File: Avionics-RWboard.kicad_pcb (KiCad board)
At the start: 2 copper layers, 90.2 x 95.9 mm, 108 parts, among them J1 282834-2, J2 200528-0100, Q1 NX3008NBKS, Q10 MBT2222ADW1T1, Q11 NX3008NBKS, Q12 MBT2222ADW1T1, Q2 MBT2222ADW1T1, Q3 NX3008NBKS, Q4 MBT2222ADW1T1, Q5 IRLML2803, Q9 NX3008NBKS, U2 TPS259621DDA, U4 ADM1176-1ARMZ-R7

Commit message: Layout mostly complete
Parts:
- removed C29: 10u, Capacitor_SMD:C_1206_3216Metric_Pad1.33x1.80mm_HandSolder
- removed kibuzzard-67C0A908: G***, kibuzzard-67C0A908
- added C31: 10uF, Capacitor_SMD:C_0603_1608Metric, F.Cu at (156.6, 113.5)
- added C36: 10uF, Capacitor_SMD:C_0603_1608Metric, F.Cu at (157.5, 119.5)
- added D8: ESD9X3.3ST5G, Diode_SMD:D_SOD-923, F.Cu at (157.9, 123.0)
- added L1: 1UH, Argus_RW_Library:HCM1A1104V2, F.Cu at (152.9, 77.0)
- added M1: ~, Argus_RW_Library:Reaction_Wheel, B.Cu at (138.1, 93.6)
- added Q6: SiRA99DP, Argus-Miscellaneous:PowerPAK SO-8, F.Cu at (142.4, 63.9)
- added R18: 0R, Resistor_SMD:R_0402_1005Metric_Pad0.72x0.64mm_HandSolder, F.Cu at (133.0, 127.5)
- added R19: 0R, Resistor_SMD:R_0402_1005Metric_Pad0.72x0.64mm_HandSolder, F.Cu at (132.4, 128.1)
- added R51: 0R, Resistor_SMD:R_0603_1608Metric, F.Cu at (157.5, 121.5)
- added R52: 0R, Resistor_SMD:R_2512_6332Metric_Pad1.40x3.35mm_HandSolder, F.Cu at (130.9, 60.5)
- added R53: 0R, Resistor_SMD:R_2512_6332Metric_Pad1.40x3.35mm_HandSolder, F.Cu at (156.4, 60.5)
- added R54: 0R, Resistor_SMD:R_0402_1005Metric_Pad0.72x0.64mm_HandSolder, F.Cu at (142.4, 94.2)
- added R55: 0R, Resistor_SMD:R_0402_1005Metric_Pad0.72x0.64mm_HandSolder, F.Cu at (142.4, 95.3)
- added R56: 0R, Resistor_SMD:R_0402_1005Metric_Pad0.72x0.64mm_HandSolder, F.Cu at (142.1, 71.6)
- added R57: 0R, Resistor_SMD:R_0402_1005Metric_Pad0.72x0.64mm_HandSolder, F.Cu at (141.5, 71.0)
- added R58: 0R, Resistor_SMD:R_0402_1005Metric_Pad0.72x0.64mm_HandSolder, F.Cu at (150.1, 91.8)
- added TP1: ~, Argus_RW_Library:KEYSTONE_5001, F.Cu at (162.9, 60.5)
- added TP10: ~, Argus_RW_Library:KEYSTONE_5001, F.Cu at (144.0, 86.5)
- added TP11: ~, Argus_RW_Library:KEYSTONE_5001, F.Cu at (158.3, 126.5)
- added TP2: ~, Argus_RW_Library:KEYSTONE_5001, F.Cu at (149.1, 60.5)
- added TP3: ~, Argus_RW_Library:KEYSTONE_5001, F.Cu at (137.5, 60.5)
- added TP4: ~, Argus_RW_Library:KEYSTONE_5001, F.Cu at (119.3, 60.5)
- added TP5: ~, Argus_RW_Library:KEYSTONE_5001, F.Cu at (158.0, 109.6)
- added TP6: ~, Argus_RW_Library:KEYSTONE_5001, F.Cu at (139.0, 111.0)
- added TP7: ~, Argus_RW_Library:KEYSTONE_5001, F.Cu at (139.8, 86.5)
- added TP8: ~, Argus_RW_Library:KEYSTONE_5001, F.Cu at (126.9, 133.0)
- added TP9: ~, Argus_RW_Library:KEYSTONE_5001, F.Cu at (147.3, 86.5)
- added U1: MCF8315C1VQRGFRQ1, Argus_RW_Library:VQFN40_RGF_TEX, F.Cu at (148.4, 95.8)
- added U3: NCP730BMT330TBG, Argus_RW_Library:WDFN6-2x2_511BR_OSI, F.Cu at (157.4, 116.5)
- F1: value 2000mA -> 3000mA
- R14, R26: value 10k -> 0R; footprint Resistor_SMD:R_0603_1608Metric -> Resistor_SMD:R_0402_1005Metric_Pad0.72x0.64mm_HandSolder
- R24, R25, R31, R46, R47: footprint Resistor_SMD:R_0603_1608Metric -> Resistor_SMD:R_0402_1005Metric_Pad0.72x0.64mm_HandSolder
- R32: value 0.05R -> 0.01R
- moved R9 145.7 mm to (119.3, 108.1), turned to 90 degrees
- moved R11 145.2 mm to (119.3, 103.2), turned to -90 degrees
- moved R12 143.5 mm to (121.2, 109.8), turned to -90 degrees
- moved R10 142.3 mm to (122.2, 96.5), turned to 180 degrees
- moved R8 138.5 mm to (122.2, 98.5), turned to 180 degrees
- moved R7 138.5 mm to (122.0, 104.0)
- moved U2 137.0 mm to (120.4, 71.1), turned to -90 degrees
- moved C2 134.0 mm to (123.0, 109.8), turned to -90 degrees
- moved J2 133.2 mm to (138.1, 131.2)
- moved R37 132.2 mm to (99.4, 103.1), turned to -90 degrees
- moved R4 131.4 mm to (129.3, 103.1), turned to -90 degrees
- moved R38 130.9 mm to (101.3, 109.8), turned to -90 degrees
- moved Q4 130.4 mm to (122.2, 101.1), turned to 180 degrees
- moved Q3 130.3 mm to (122.1, 106.6)
- moved R5 129.9 mm to (131.2, 109.8), turned to -90 degrees
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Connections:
- net Net-(D5-K) renamed /Power/SWITCHED_POWER
- net Net-(Q6-S) renamed /Power/FUSED_POWER
- net SYSTEM_VDD renamed VMAIN
- C6 pad 2: Net-(U2-OUT) -> /Power/eFUSED_POWER
- J2 pad 1: GND -> SYS_3V3
- R24 pad 1: GND -> /Power/eFUSED_POWER
- R25 pad 2: /Power/A1 -> /Power/A0
- R26 pad 1: AGND -> /Motor/BRAKE
- R26 pad 2: /Motor/DIR -> AVDD
- R32 pad 1: VM -> /Power/MON_POWER
- R32 pad 2: Net-(U2-OUT) -> /Power/eFUSED_POWER
- R33 pad 1: VM -> /Power/MON_POWER
- U2 pad 5: Net-(U2-OUT) -> /Power/eFUSED_POWER
- U4 pad 1: Net-(U2-OUT) -> /Power/eFUSED_POWER
- U4 pad 2: VM -> /Power/MON_POWER
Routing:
- net GND: track 0.00 -> 99.4 mm, vias 0 -> 77
- net /Connectors/RW_EN: track 0.00 -> 86.4 mm, vias 0 -> 2
- net VM: track 0.00 -> 84.4 mm
- net /Connectors/SCL: track 0.00 -> 75.1 mm
- net /Power/I2C Bus Protection 2/SCL_DEVICE: track 0.00 -> 72.0 mm, vias 0 -> 2
- net /Power/I2C Bus Protection 2/SDA_DEVICE: track 0.00 -> 64.7 mm, vias 0 -> 2
- net /Power/eFUSED_POWER: track 0.00 -> 63.3 mm
- net /Connectors/RW_POWER_FLT: track 0.00 -> 58.9 mm, vias 0 -> 2
- net /Connectors/SDA: track 0.00 -> 57.1 mm, vias 0 -> 2
- net /Motor/I2C Bus Protection 1/SDA_DEVICE: track 0.00 -> 48.7 mm, vias 0 -> 2
- net LOCAL_3V3: track 0.00 -> 43.0 mm
- net /Motor/I2C Bus Protection 1/SCL_DEVICE: track 0.00 -> 39.0 mm, vias 0 -> 2
- net /Connectors/RW_MOTOR_FLT: track 0.00 -> 38.0 mm, vias 0 -> 1
- net /Power/SWITCHED_POWER: track 0.00 -> 34.1 mm
- net /Connectors/RW_MOTOR_ALRM: track 0.00 -> 33.0 mm, vias 0 -> 2
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- added copper zone on In2.Cu, net +3V3
- added copper zone on F.Cu, net /Motor/SW_BUCK
- added copper zone on B.Cu, net AGND
- added copper zone on F.Cu, net AGND
- added copper zone on In1.Cu, net AGND
- added copper zone on In2.Cu, net AGND
- added copper zone on In2.Cu, net AVDD
- added copper zone on B.Cu, net GND
- added copper zone on F.Cu, net GND
- added copper zone on In1.Cu, net GND
- added copper zone on In2.Cu, net GND
- added copper zone on B.Cu, net Net-(M1-A)
- added copper zone on F.Cu, net Net-(M1-A)
- added copper zone on B.Cu, net Net-(M1-B)
- added copper zone on F.Cu, net Net-(M1-B)
- added copper zone on B.Cu, net Net-(M1-C)
- added copper zone on F.Cu, net Net-(M1-C)
- added copper zone on F.Cu, net VM
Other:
- copper layers 2 -> 4
- board text added: "ARGUS Cubesat Carnegie Mellon University Reaction Wheel Board V1.0"
- board text added: "Reaction Wheel Board V1.0"
- board text removed: "ARGUS Cubesat Carnegie Mellon University Mainboard v3.0"
- board text removed: "mainboard.v3.0"

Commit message: Update silkscreen
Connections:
- U1 pad 39: unconnected-(U1-ALARM-Pad39) -> /Connectors/RW_MOTOR_ALRM
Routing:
- net /Connectors/RW_MOTOR_ALRM: track 33.0 -> 40.2 mm
- net unconnected-(U1-ALARM-Pad39): track 5.82 -> 0.00 mm
- net GND: track 99.4 -> 102.5 mm
- net AGND: track 30.0 -> 30.5 mm, vias 5 -> 12
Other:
- board text removed: "Reaction Wheel Board V1.0"

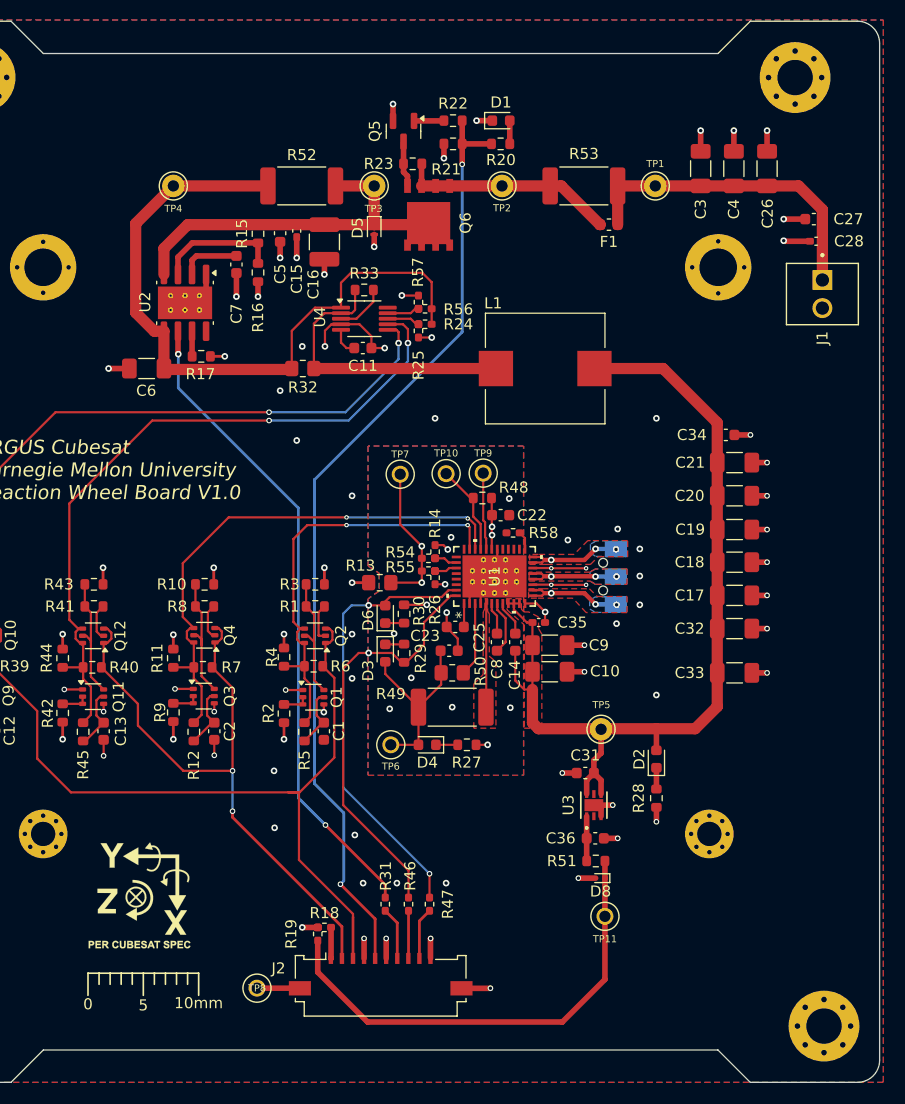
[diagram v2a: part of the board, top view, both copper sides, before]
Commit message: Push requested changes - silkscreen, copper width, pi filter
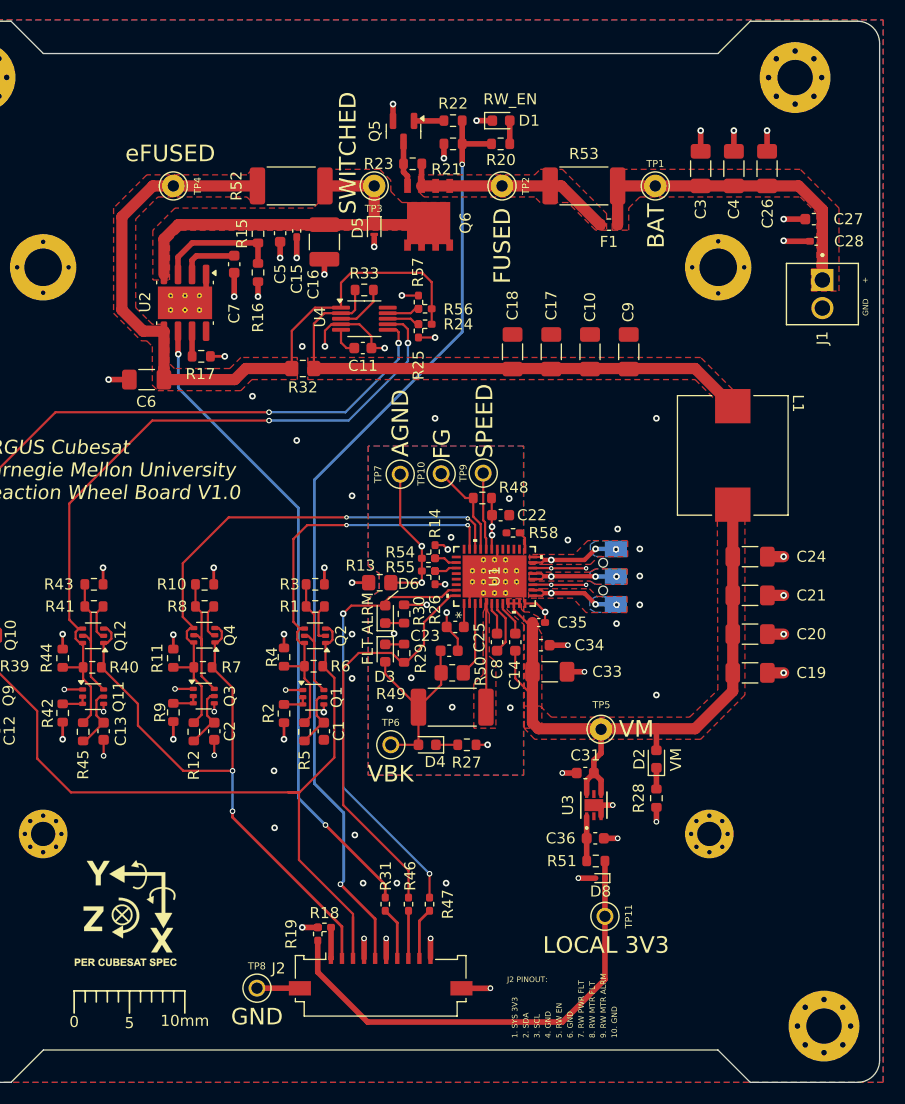
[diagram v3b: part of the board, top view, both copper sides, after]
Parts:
- removed C32: 47u, Capacitor_SMD:C_1206_3216Metric_Pad1.33x1.80mm_HandSolder
- added C24: 47u, Capacitor_SMD:C_1206_3216Metric_Pad1.33x1.80mm_HandSolder, F.Cu at (171.5, 94.0)
- moved C10 29.1 mm to (157.0, 75.5), turned to -90 degrees
- moved C18 27.6 mm to (150.0, 75.5), turned to -90 degrees
- moved C17 27.5 mm to (153.5, 75.5), turned to -90 degrees
- moved C9 27.5 mm to (160.5, 75.5), turned to -90 degrees
- moved C34 25.3 mm to (152.6, 102.0)
- moved L1 18.7 mm to (169.9, 84.8), turned to -90 degrees
- moved C33 16.7 mm to (153.4, 104.4)
- moved C19 13.0 mm to (171.5, 104.5)
- moved C20 12.6 mm to (171.5, 101.0)
- moved C21 12.1 mm to (171.5, 97.5)
- moved REF** 2.03 mm to (115.0, 126.2)
- moved REF** 2.03 mm to (110.4, 133.2)
- moved REF** 1.63 mm to (99.7, 93.5)
- moved C6 1.00 mm to (116.9, 78.0)
- moved R52 0.95 mm to (130.0, 60.5)
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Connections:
- C10 pad 2: VM -> /Power/MON_POWER
- C17 pad 2: VM -> /Power/MON_POWER
- C18 pad 2: VM -> /Power/MON_POWER
- C9 pad 2: VM -> /Power/MON_POWER
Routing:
- net /Power/MON_POWER: track 26.5 -> 49.4 mm
- net VM: track 84.4 -> 71.1 mm
- net GND: track 102.5 -> 97.5 mm, vias 77 -> 73
- net /Power/eFUSED_POWER: track 63.3 -> 66.4 mm
- net /Power/SWITCHED_POWER: track 34.1 -> 35.6 mm
- net /Motor/FG: track 8.27 -> 9.17 mm
- net /Connectors/RW_MOTOR_FLT: vias 1 -> 0
- added copper zone on F.Cu, net /Power/FUSED_POWER
- added copper zone on F.Cu, net /Power/MON_POWER
- added copper zone on F.Cu, net /Power/SWITCHED_POWER
- added copper zone on F.Cu, net /Power/eFUSED_POWER
- added copper zone on F.Cu, net VMAIN
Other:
- board text added: "+"
- board text added: "1. SYS 3V3"
- board text added: "10. GND"
- board text added: "2. SDA"
- board text added: "3. SCL"
- board text added: "4. GND"
- board text added: "5. RW EN"
- board text added: "6. GND"
- board text added: "7. RW PWR FLT"
- board text added: "8. RW MTR FLT"
- board text added: "9. RW MTR ALRM"
- board text added: "AGND"
- board text added: "ALRM"
- board text added: "BAT"
- board text added: "FG"
- board text added: "FLT"
- board text added: "FUSED"
- board text added: "GND"
- board text added: "J2 PINOUT:"
- board text added: "LOCAL 3V3"
- board text added: "RW_EN"
- board text added: "SPEED"
- board text added: "SWITCHED"
- board text added: "VBK"
- board text added: "VM"
- board text added: "eFUSED"

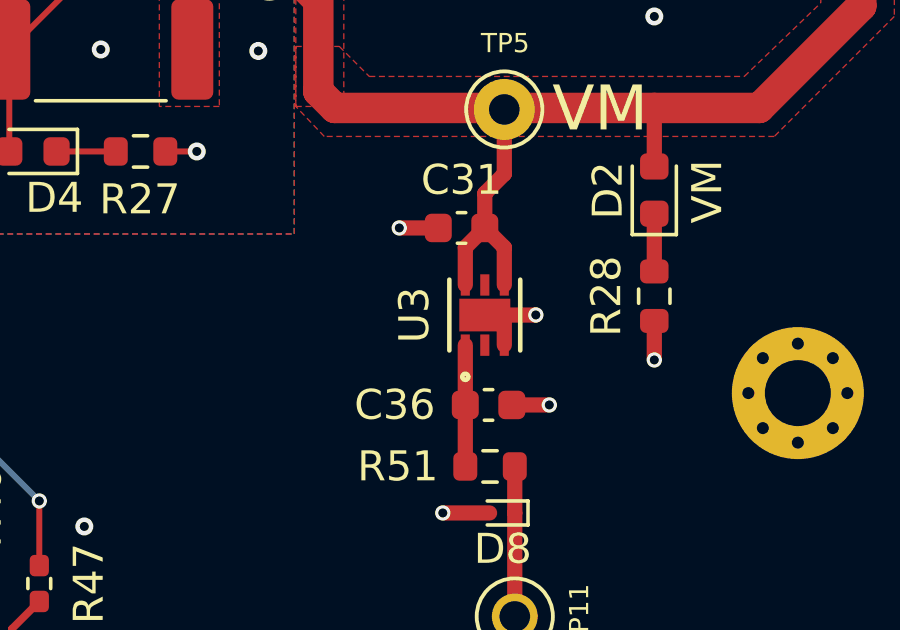
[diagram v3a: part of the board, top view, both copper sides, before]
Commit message: Add and correct BOM for easy Digikey ordering
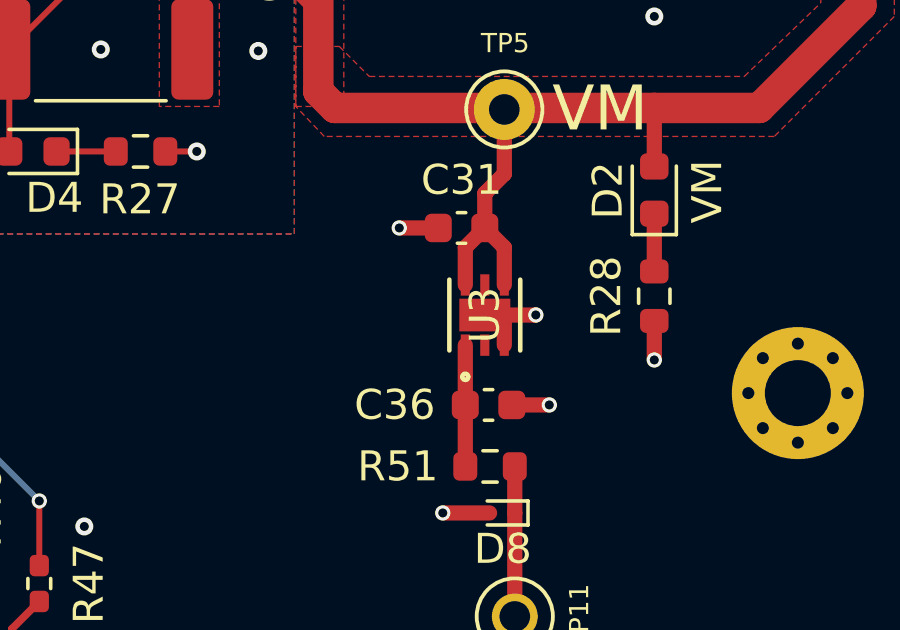
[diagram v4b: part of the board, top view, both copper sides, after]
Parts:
- C1, C12, C13, C2: value 10nF -> 10n
- C11: value 3n3 -> 3.3n
- C15: value 0.1u -> 100n
- C31, C36: value 10uF -> 10u
- C8: value 47nF -> 47n
- D1: value GREEN -> GREEN LED
- M1: value ~ -> 304D-262503
- R30: value 470 -> 470R
- R33: value 1K -> 1k
- TP1, TP10, TP11, TP2, TP3, TP4, TP5, TP6, TP7, TP8, TP9: value ~ -> TP

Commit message: Local Stash
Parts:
- moved REF** 28.6 mm to (71.6, 98.8), turned to 180 degrees
